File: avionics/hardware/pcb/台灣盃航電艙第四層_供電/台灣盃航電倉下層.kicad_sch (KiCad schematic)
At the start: 42 parts, among them J1 XT60, J2 XT60, J4 Pyro1, J5 Pyro2, Q1 NMOS, Q2 NMOS, Q3 NMOS, Q4 NMOS, U3 LM2596S-5, U4 LM2596S-5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

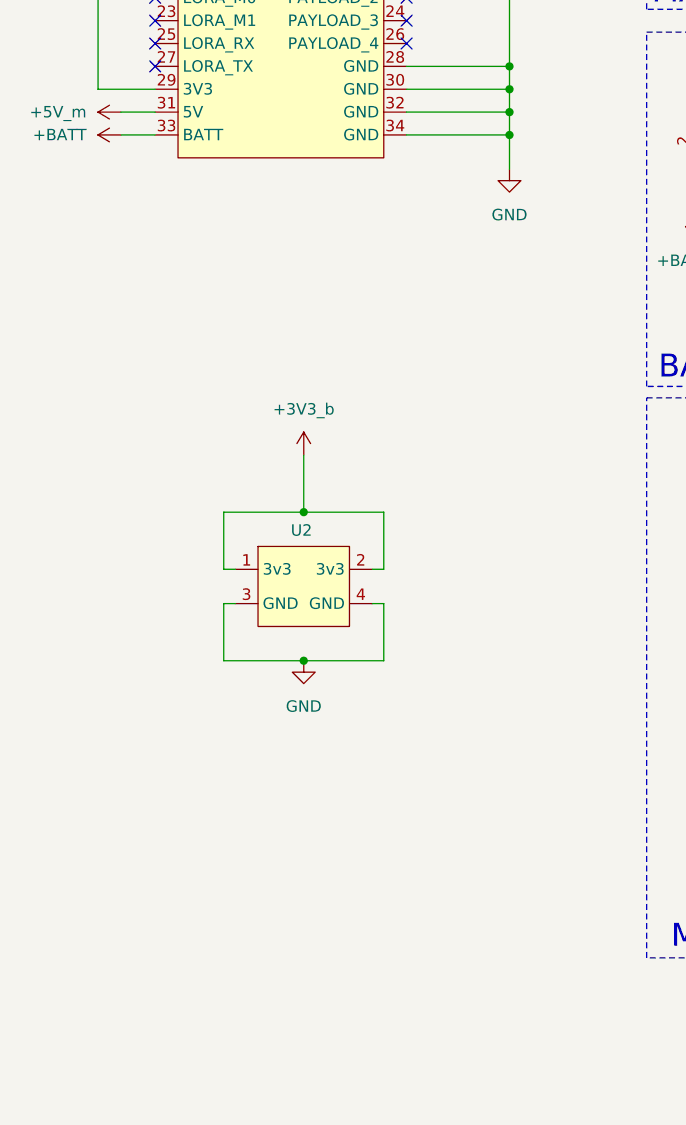
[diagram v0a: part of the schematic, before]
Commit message: 上傳新的連接器
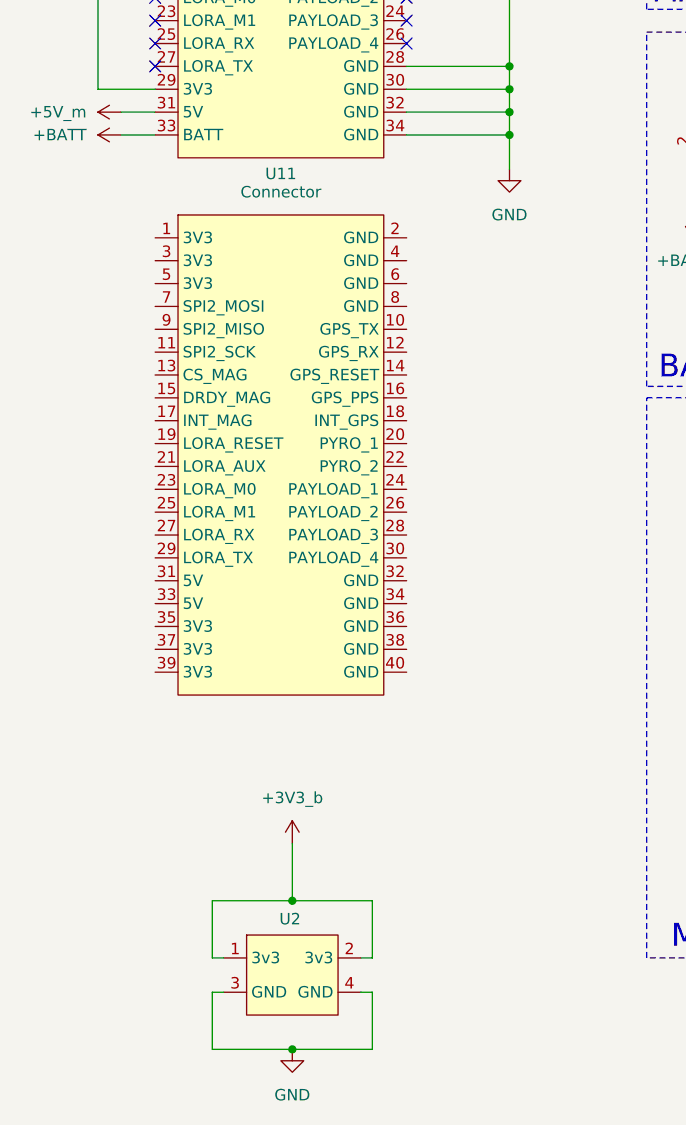
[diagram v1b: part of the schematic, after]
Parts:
- added U11: Connector, symbol MySymbol:2*20 PC104
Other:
- moved on the sheet: U2
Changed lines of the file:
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@@
 	)
 	(junction
-		(at 46.99 125.73)
+		(at 45.72 168.91)
 		(diameter 0)
 		(color 0 0 0 0)
@@
 	)
 	(junction
-		(at 46.99 109.22)
+		(at 45.72 152.4)
 		(diameter 0)
 		(color 0 0 0 0)
@@
 	(wire
 		(pts
-			(xy 39.37 119.38) (xy 38.1 119.38)
+			(xy 38.1 162.56) (xy 36.83 162.56)
 		)
 		(stroke
@@
 	(wire
 		(pts
-			(xy 46.99 102.87) (xy 46.99 109.22)
+			(xy 45.72 146.05) (xy 45.72 152.4)
 		)
 		(stroke
@@
 	(wire
 		(pts
-			(xy 55.88 125.73) (xy 55.88 119.38)
+			(xy 54.61 168.91) (xy 54.61 162.56)
 		)
 		(stroke
@@
 	(wire
 		(pts
-			(xy 46.99 125.73) (xy 55.88 125.73)
+			(xy 45.72 168.91) (xy 54.61 168.91)
 		)
 		(stroke
@@
 	(wire
 		(pts
-			(xy 55.88 115.57) (xy 54.61 115.57)
+			(xy 54.61 158.75) (xy 53.34 158.75)
 		)
 		(stroke
@@
 	(wire
 		(pts
-			(xy 38.1 115.57) (xy 38.1 109.22)
+			(xy 36.83 158.75) (xy 36.83 152.4)
 		)
 		(stroke
@@
 	(wire
 		(pts
-			(xy 38.1 119.38) (xy 38.1 125.73)
+			(xy 36.83 162.56) (xy 36.83 168.91)
 		)
 		(stroke
@@
 	(wire
 		(pts
-			(xy 54.61 119.38) (xy 55.88 119.38)
+			(xy 53.34 162.56) (xy 54.61 162.56)
 		)
 		(stroke
@@
 	(wire
 		(pts
-			(xy 55.88 109.22) (xy 55.88 115.57)
+			(xy 54.61 152.4) (xy 54.61 158.75)
 		)
 		(stroke
@@
 	(wire
 		(pts
-			(xy 39.37 115.57) (xy 38.1 115.57)
+			(xy 38.1 158.75) (xy 36.83 158.75)
 		)
 		(stroke
@@
 	(wire
 		(pts
-			(xy 38.1 125.73) (xy 46.99 125.73)
+			(xy 36.83 168.91) (xy 45.72 168.91)
 		)
 		(stroke
@@
 	(wire
 		(pts
-			(xy 38.1 109.22) (xy 46.99 109.22)
+			(xy 36.83 152.4) (xy 45.72 152.4)
 		)
 		(stroke
@@
 	(wire
 		(pts
-			(xy 46.99 109.22) (xy 55.88 109.22)
+			(xy 45.72 152.4) (xy 54.61 152.4)
 		)
 		(stroke
@@
 	)
 	(symbol
+		(lib_id "MySymbol:2*20 PC104")
+		(at 44.45 74.93 0)
+		(unit 1)
+		(exclude_from_sim no)
+		(in_bom yes)
+		(on_board yes)
+		(dnp no)
+		(property "Reference" "U11"
+			(at 44.45 71.628 0)
+			(effects
+				(font
+					(size 1.27 1.27)
+				)
+			)
+		)
+		(property "Value" "Connector"
+			(at 44.45 73.66 0)
+			(effects
+				(font
+					(size 1.27 1.27)
+				)
+			)
+		)
+		(property "Footprint" ""
+			(at 44.45 74.93 0)
+			(effects
+				(font
+					(size 1.27 1.27)
+				)
+				(hide yes)
+			)
+		)
+		(property "Datasheet" ""
+			(at 44.45 74.93 0)
+			(effects
+				(font
+					(size 1.27 1.27)
+				)
+				(hide yes)
+			)
+		)
+		(property "Description" ""
+			(at 44.45 74.93 0)
+			(effects
+				(font
+					(size 1.27 1.27)
+				)
+				(hide yes)
+			)
+		)
+		(pin "19"
+		)
+		(pin "39"
+		)
+		(pin "9"
+		)
+		(pin "15"
+		)
+		(pin "11"
+		)
+		(pin "7"
+		)
+		(pin "29"
+		)
+		(pin "31"
+		)
+		(pin "5"
+		)
+		(pin "4"
+		)
+		(pin "1"
+		)
+		(pin "21"
+		)
+		(pin "12"
+		)
+		(pin "27"
+		)
+		(pin "16"
+		)
+		(pin "20"
+		)
+		(pin "23"
+		)
+		(pin "13"
+		)
+		(pin "17"
+		)
+		(pin "3"
+		)
+		(pin "25"
+		)
+		(pin "33"
+		)
+		(pin "35"
+		)
+		(pin "37"
+		)
+		(pin "6"
+		)
+		(pin "2"
+		)
+		(pin "8"
+		)
+		(pin "14"
+		)
+		(pin "18"
+		)
+		(pin "10"
+		)
+		(pin "24"
+		)
+		(pin "26"
+		)
+		(pin "32"
+		)
+		(pin "34"
+		)
+		(pin "36"
+		)
+		(pin "38"
+		)
+		(pin "28"
+		)
+		(pin "30"
+		)
+		(pin "22"
+		)
+		(pin "40"
+		)
+		(instances
+			(project "台灣盃航電倉下層"
+				(path "/d6ad6b2d-1383-4789-a012-4f2c1ad930c7"
+					(reference "U11")
+					(unit 1)
+				)
+			)
+		)
+	)
+	(symbol
 		(lib_id "Device:LED")
 		(at 184.15 140.97 90)
@@
 	(symbol
 		(lib_id "power:+3V3")
-		(at 46.99 102.87 0)
+		(at 45.72 146.05 0)
 		(unit 1)
 		(exclude_from_sim no)
@@
 		(fields_autoplaced yes)
 		(property "Reference" "#PWR02"
-			(at 46.99 106.68 0)
+			(at 45.72 149.86 0)
 			(effects
 				(font
@@
 		)
 		(property "Value" "+3V3_b"
-			(at 46.99 97.79 0)
+			(at 45.72 140.97 0)
 			(effects
 				(font
@@
 		)
 		(property "Footprint" ""
-			(at 46.99 102.87 0)
+			(at 45.72 146.05 0)
 			(effects
 				(font
@@
 		)
 		(property "Datasheet" ""
-			(at 46.99 102.87 0)
+			(at 45.72 146.05 0)
 			(effects
 				(font
@@
 		)
 		(property "Description" "Power symbol creates a global label with name \"+3V3\""
-			(at 46.99 102.87 0)
+			(at 45.72 146.05 0)
 			(effects
 				(font
@@
 	(symbol
 		(lib_id "power:GND")
-		(at 46.99 125.73 0)
+		(at 45.72 168.91 0)
 		(unit 1)
 		(exclude_from_sim no)
@@
 		(fields_autoplaced yes)
 		(property "Reference" "#PWR03"
-			(at 46.99 132.08 0)
+			(at 45.72 175.26 0)
 			(effects
 				(font
@@
 		)
 		(property "Value" "GND"
-			(at 46.99 130.81 0)
+			(at 45.72 173.99 0)
 			(effects
 				(font
@@
 		)
 		(property "Footprint" ""
-			(at 46.99 125.73 0)
+			(at 45.72 168.91 0)
 			(effects
 				(font
@@
 		)
 		(property "Datasheet" ""
-			(at 46.99 125.73 0)
+			(at 45.72 168.91 0)
 			(effects
 				(font
@@
 		)
 		(property "Description" "Power symbol creates a global label with name \"GND\" , ground"
-			(at 46.99 125.73 0)
+			(at 45.72 168.91 0)
 			(effects
 				(font
@@
 	(symbol
 		(lib_id "MySymbol:2x2排針連接")
-		(at 46.99 113.03 0)
+		(at 45.72 156.21 0)
 		(unit 1)
 		(exclude_from_sim no)
@@
 		(dnp no)
 		(property "Reference" "U2"
-			(at 46.736 111.252 0)
+			(at 45.466 154.432 0)
 			(effects
 				(font
@@
 		)
 		(property "Value" "~"
-			(at 46.99 111.252 0)
+			(at 45.72 154.432 0)
 			(effects
 				(font
@@
 		)
 		(property "Footprint" "Connector_PinHeader_1.00mm:PinHeader_2x02_P1.00mm_Vertical"
-			(at 46.99 113.03 0)
+			(at 45.72 156.21 0)
 			(effects
 				(font
@@
 		)
 		(property "Datasheet" ""
-			(at 46.99 113.03 0)
+			(at 45.72 156.21 0)
 			(effects
 				(font
@@
 		)
 		(property "Description" ""
-			(at 46.99 113.03 0)
+			(at 45.72 156.21 0)
 			(effects
 				(font

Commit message: Add files via upload
change schematics
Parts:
- removed U7: ~, Connector_PinHeader_1.00mm:PinHeader_2x17_P1.00mm_Vertical, symbol MySymbol:2x17排針母座連接
- U11: footprint (none) -> Connector_PinHeader_2.54mm:PinHeader_2x20_P2.54mm_Vertical
- U2: footprint Connector_PinHeader_1.00mm:PinHeader_2x02_P1.00mm_Vertical -> Connector_PinHeader_2.54mm:PinHeader_2x02_P2.54mm_Vertical
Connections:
- net +3V3_m: now also U11.1 (3V3), U11.3 (3V3), U11.35 (3V3), U11.37 (3V3), U11.39 (3V3), U11.5 (3V3)
- net +5V_m: now also U11.31 (5V), U11.33 (5V)
- net GND: now also U11.2 (GND), U11.32 (GND), U11.34 (GND), U11.36 (GND), U11.38 (GND), U11.4 (GND), U11.40 (GND), U11.6 (GND), U11.8 (GND)
- net PYRO1: now also U11.20 (PYRO_1)
- net PYRO2: now also U11.22 (PYRO_2)
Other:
- moved on the sheet: U11, U2
